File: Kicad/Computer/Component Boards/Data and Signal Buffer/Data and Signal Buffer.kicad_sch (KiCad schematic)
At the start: 20 parts, among them CN1 CA0612KRX7R9BB100, CN2 CA0612KRX7R9BB100, CN3 CA0612KRX7R9BB100, CN4 CA0612KRX7R9BB100, IC1 SN74ABT245BDBR, IC2 SN74ABT245BDBR, IC5 AP7365-33WG-7, J2 Conn_02x20_Counter_Clockwise

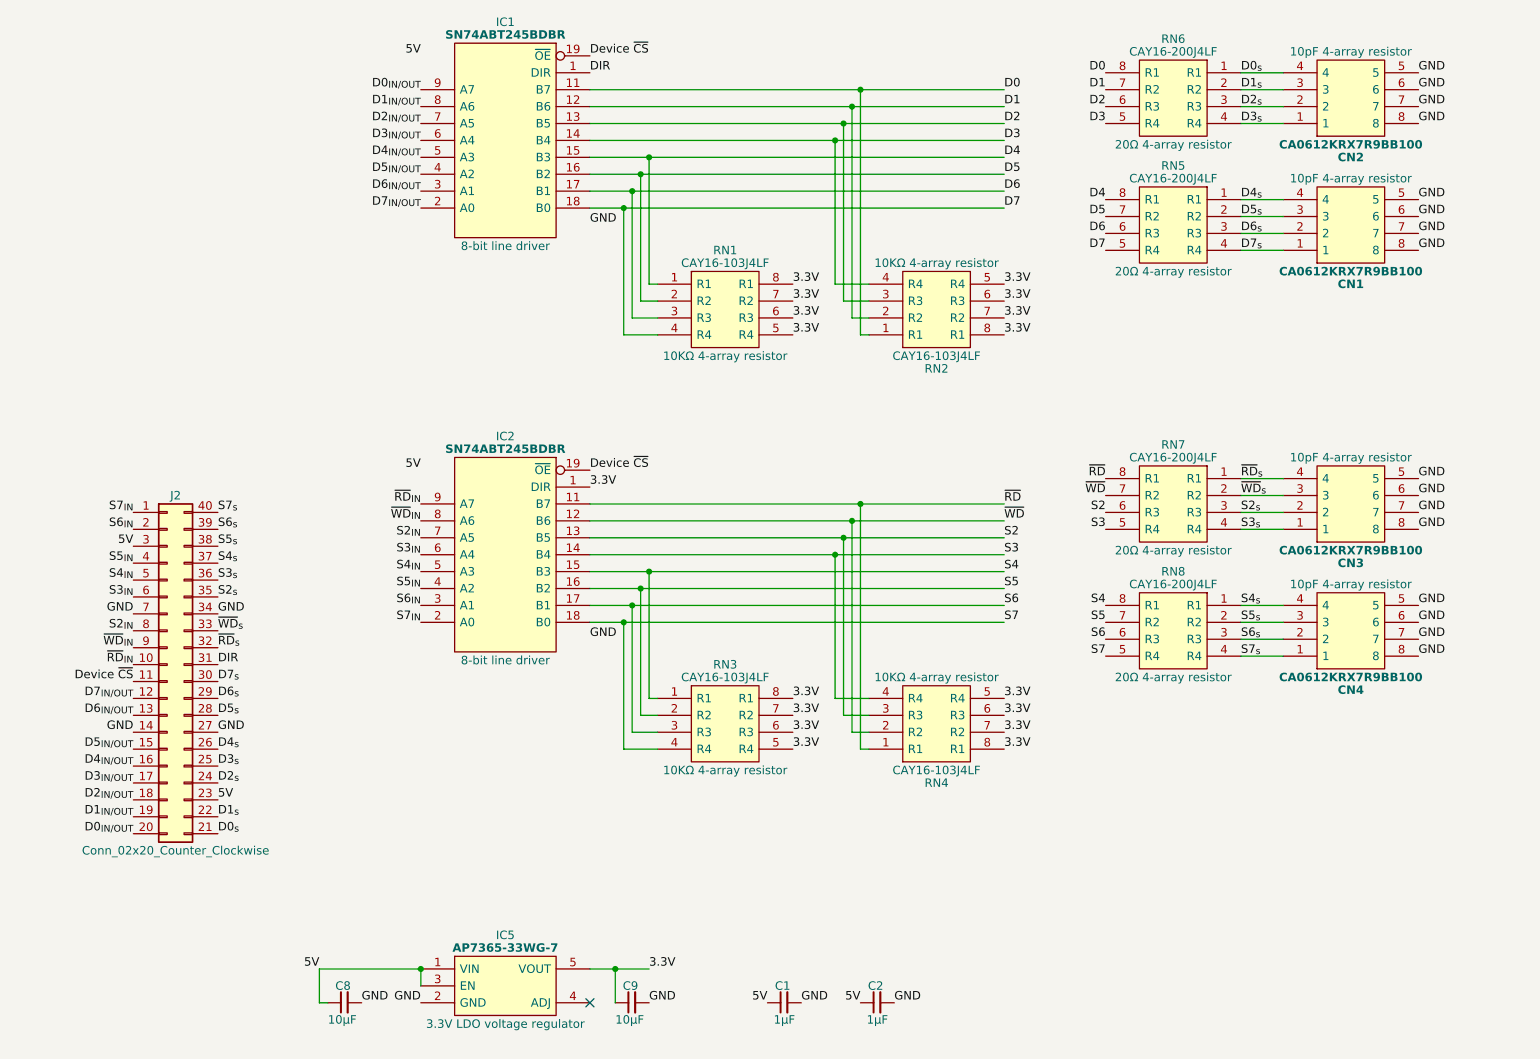
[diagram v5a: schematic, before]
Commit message: Converted more PCBs to Kicad 8.
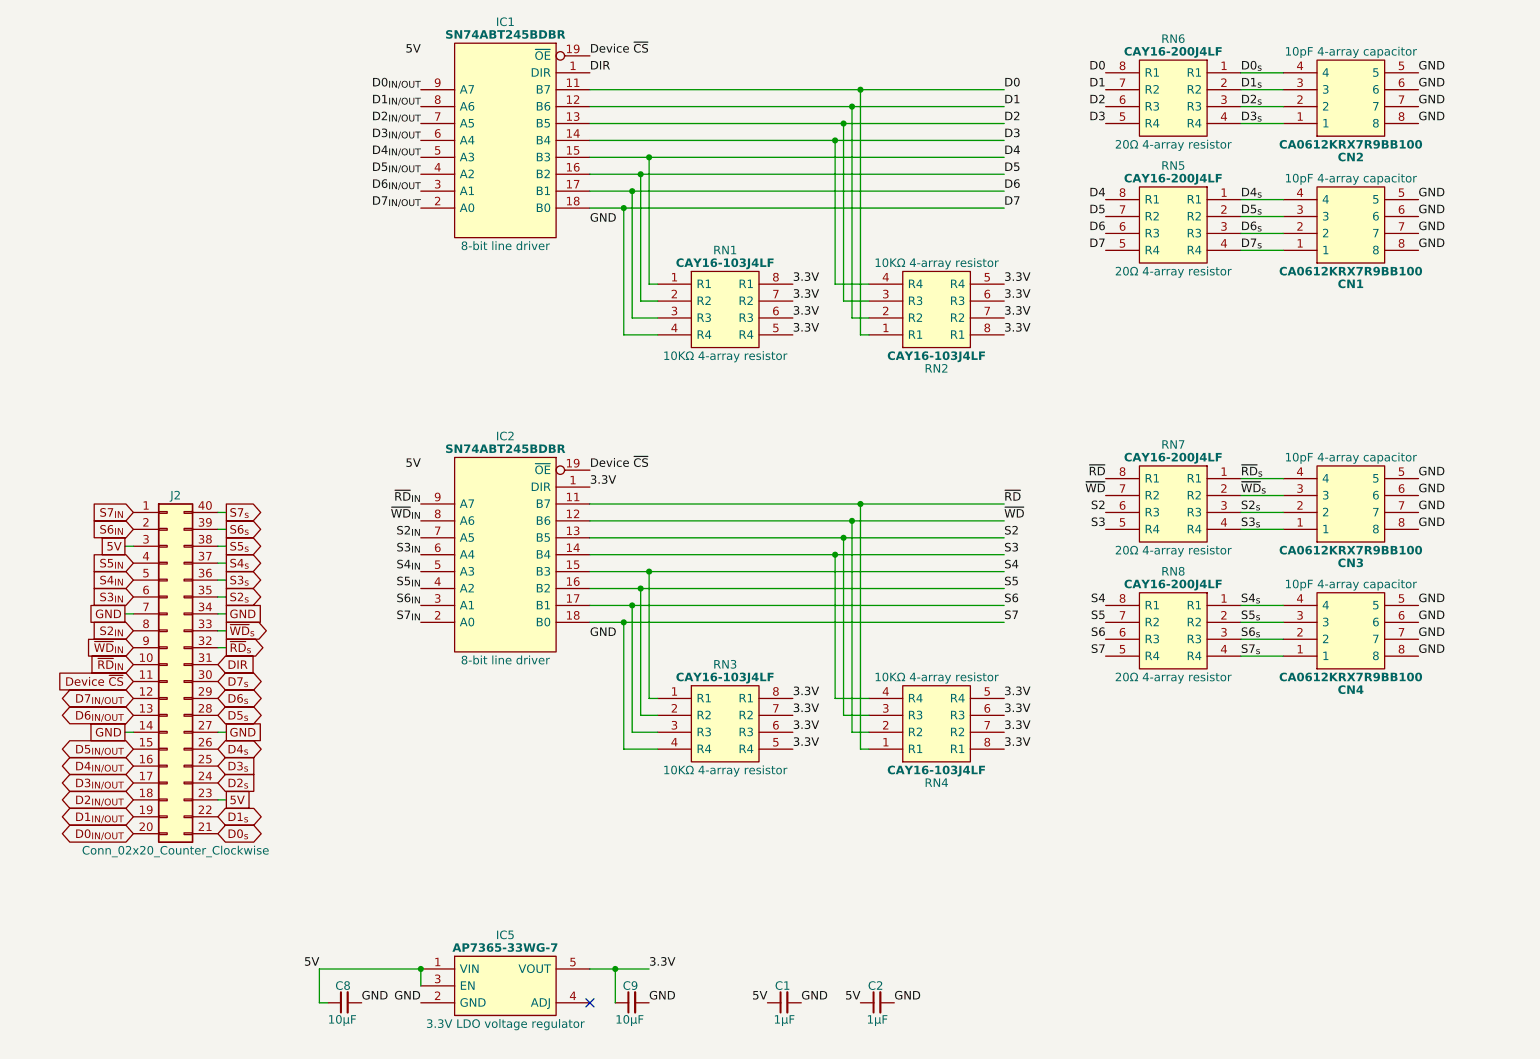
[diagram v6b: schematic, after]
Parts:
- C1, C2, C8, C9: Garbage (none) -> Unpolarized capacitor, small symbol
- CN1, CN2, CN3, CN4: Garbage (none) -> Capacitor,ceramic,multilayer,SMT,50V,10pF
- IC1, IC2: footprint SOP65P780X200-20N -> SamacSys_Parts:SOP65P780X200-20N; Garbage (none) -> Texas Instruments SN74ABT245BDBR, Bus Transceiver, 8-Bit No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
- IC5: footprint SOT95P285X130-5N -> SamacSys_Parts:SOT95P285X130-5N; Garbage (none) -> DiodesZetex AP7365-33WG-7, LDO Voltage Regulator, 600mA, 3.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
- RN1, RN2, RN3, RN4: Garbage (none) -> Bourns CAY16 Series 4.7k +/-5% Isolated SMT Resistor Array,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
- RN5, RN6, RN7, RN8: Garbage (none) -> Bourns CAY16 Series 20 +/-5% Isolated SMT Resistor Array, 4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

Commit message: Panelised Speed Board.
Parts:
- C1, C2, C8, C9: Garbage Unpolarized capacitor, small symbol -> (none)
- CN1, CN2, CN3, CN4: Garbage Capacitor,ceramic,multilayer,SMT,50V,10pF -> (none)
- IC5: Garbage DiodesZetex AP7365-33WG-7, LDO Voltage Regulator, 600mA, 3.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 -> (none)
- RN1, RN2, RN3, RN4: Garbage Bourns CAY16 Series 4.7k +/-5% Isolated SMT Resistor Array,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 -> (none)
- RN5, RN6, RN7, RN8: Arrow Part Number CAY16-331J4LF -> (none); Arrow Price/Stock https://www.arrow.com/en/products/cay16-331j4lf/bourns?regi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 -> (none); Garbage Bourns CAY16 Series 20 +/-5% Isolated SMT Resistor Array, 4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 -> (none)

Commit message: Use VRML instead of STEPs for Processor Board models.
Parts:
- added J1, J3: Pin_Header_01x20, SamacSys_Parts:PinHeader_1x20_P2.54mm_Vertical, symbol HCP65:Pin_Header_01x32
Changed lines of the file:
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@@
+	)
+	(symbol
+		(lib_id "HCP65:Pin_Header_01x32")
+		(at 52.07 95.25 0)
+		(mirror y)
+		(unit 1)
+		(exclude_from_sim no)
+		(in_bom yes)
+		(on_board yes)
+		(dnp no)
+		(property "Reference" "J1"
+			(at 52.07 93.98 0)
+			(effects
+				(font
+					(size 1.27 1.27)
+				)
+			)
+		)
+		(property "Value" "Pin_Header_01x20"
+			(at 52.07 96.52 0)
+			(effects
+				(font
+					(size 1.27 1.27)
+				)
+			)
+		)
+		(property "Footprint" "SamacSys_Parts:PinHeader_1x20_P2.54mm_Vertical"
+			(at 52.07 99.06 0)
+			(effects
+				(font
+					(size 1.27 1.27)
+				)
+				(hide yes)
+			)
+		)
+		(property "Datasheet" "~"
+			(at 57.15 95.25 0)
+			(effects
+				(font
+					(size 1.27 1.27)
+				)
+				(hide yes)
+			)
+		)
+		(property "Description" ""
+			(at 52.07 95.25 0)
+			(effects
+				(font
+					(size 1.27 1.27)
+				)
+				(hide yes)
+			)
+		)
+		(instances
+			(project "Data and Signal Buffer"
+				(path "/337b5f72-8be1-4121-9dc6-479b565482b2"
+					(reference "J1")
+					(unit 1)
+				)
+			)
+		)
+	)
+	(symbol
+		(lib_id "HCP65:Pin_Header_01x32")
+		(at 52.07 100.33 0)
+		(unit 1)
+		(exclude_from_sim no)
+		(in_bom yes)
+		(on_board yes)
+		(dnp no)
+		(property "Reference" "J3"
+			(at 52.07 99.06 0)
+			(effects
+				(font
+					(size 1.27 1.27)
+				)
+			)
+		)
+		(property "Value" "Pin_Header_01x20"
+			(at 52.07 101.6 0)
+			(effects
+				(font
+					(size 1.27 1.27)
+				)
+			)
+		)
+		(property "Footprint" "SamacSys_Parts:PinHeader_1x20_P2.54mm_Vertical"
+			(at 52.07 104.14 0)
+			(effects
+				(font
+					(size 1.27 1.27)
+				)
+				(hide yes)
+			)
+		)
+		(property "Datasheet" "~"
+			(at 46.99 100.33 0)
+			(effects
+				(font
+					(size 1.27 1.27)
+				)
+				(hide yes)
+			)
+		)
+		(property "Description" ""
+			(at 52.07 100.33 0)
+			(effects
+				(font
+					(size 1.27 1.27)
+				)
+				(hide yes)
+			)
+		)
+		(instances
+			(project "Data and Signal Buffer"
+				(path "/337b5f72-8be1-4121-9dc6-479b565482b2"
+					(reference "J3")
+					(unit 1)
+				)
+			)
+		)
 	)
 	(symbol
